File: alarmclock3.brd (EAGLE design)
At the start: 81 x 80 mm, 28 parts, among them X1 MKDSN1,5/2-5,08, X2 MKDSN1,5/2-5,08

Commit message: route 100%
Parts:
- removed C1: (no value), SparkFun-Passives:CPOL-RADIAL-1000UF-63V
- added C11: 330uF/25V, SparkFun-Passives:CPOL-RADIAL-10UF-25V
- moved C10 15.7 mm to (34.5, 30.5)
- moved C4 8.89 mm to (25.4, 22.9)
- moved R5 3.45 mm to (28.7, 26.9)
- moved R2 2.54 mm to (38.1, 30.5)
- moved C14 2.54 mm to (25.4, 49.5)
- moved C9 2.54 mm to (33.0, 50.8)
- moved C8 2.40 mm to (27.9, 49.0)
- moved C13 2.18 mm to (31.8, 26.2)
- moved C7 1.27 mm to (29.7, 30.7)
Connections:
- net GND: now also C11.2; no longer C1.2
- net N$3: now also C11.1; no longer C1.1
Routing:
- net N$2: track 122.7 -> 49.8 mm
- net N$1: track 0.00 -> 58.3 mm, vias 0 -> 1
- net GND: track 297.0 -> 241.2 mm
- net N$27: track 8.62 -> 61.0 mm
- net N$23: track 77.9 -> 29.6 mm, vias 0 -> 2
- net N$8: track 2.54 -> 30.9 mm, vias 0 -> 1
- net N$3: track 114.3 -> 97.5 mm
- net N$25: track 17.4 -> 1.86 mm
- net N$12: track 0.00 -> 13.6 mm, vias 0 -> 2
- net N$6: track 47.5 -> 55.3 mm, vias 1 -> 2
- net VCC: track 53.8 -> 60.4 mm, vias 0 -> 2
- net N$10: track 29.9 -> 36.4 mm, vias 0 -> 2
- net N$11: track 0.00 -> 6.11 mm
- net N$22: track 4.03 -> 9.95 mm
- net N$13: track 28.0 -> 33.5 mm
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
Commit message: !00% routable
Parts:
- moved U$1 6.90 mm to (14.5, 70.6), turned to 270 degrees
- moved U$4 6.86 mm to (65.0, 17.0)
- moved U$2 6.61 mm to (24.4, 72.6)
- moved U$5 6.61 mm to (6.10, 47.2)
- moved C6 3.31 mm to (65.0, 35.1)
- moved X2 2.84 mm to (71.6, 35.8)
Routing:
- net N$27: track 61.0 -> 15.2 mm, vias 2 -> 4
- net N$4: track 88.1 -> 50.0 mm
- net N$10: track 36.4 -> 73.6 mm, vias 2 -> 0
- net N$1: track 58.3 -> 81.5 mm, vias 1 -> 3
- net N$8: track 30.9 -> 37.0 mm
- net N$6: track 55.3 -> 60.6 mm
- net N$18: track 16.2 -> 20.0 mm
- net N$15: track 5.26 -> 8.45 mm, vias 0 -> 2
- net N$17: track 4.73 -> 7.39 mm, vias 0 -> 2
- net GND: track 241.2 -> 243.8 mm
- net N$5: track 49.5 -> 47.0 mm
- net N$23: track 29.6 -> 28.2 mm
- net N$9: track 16.1 -> 15.0 mm
- net N$16: track 37.7 -> 36.6 mm, vias 3 -> 2
- net N$3: track 97.5 -> 98.5 mm
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
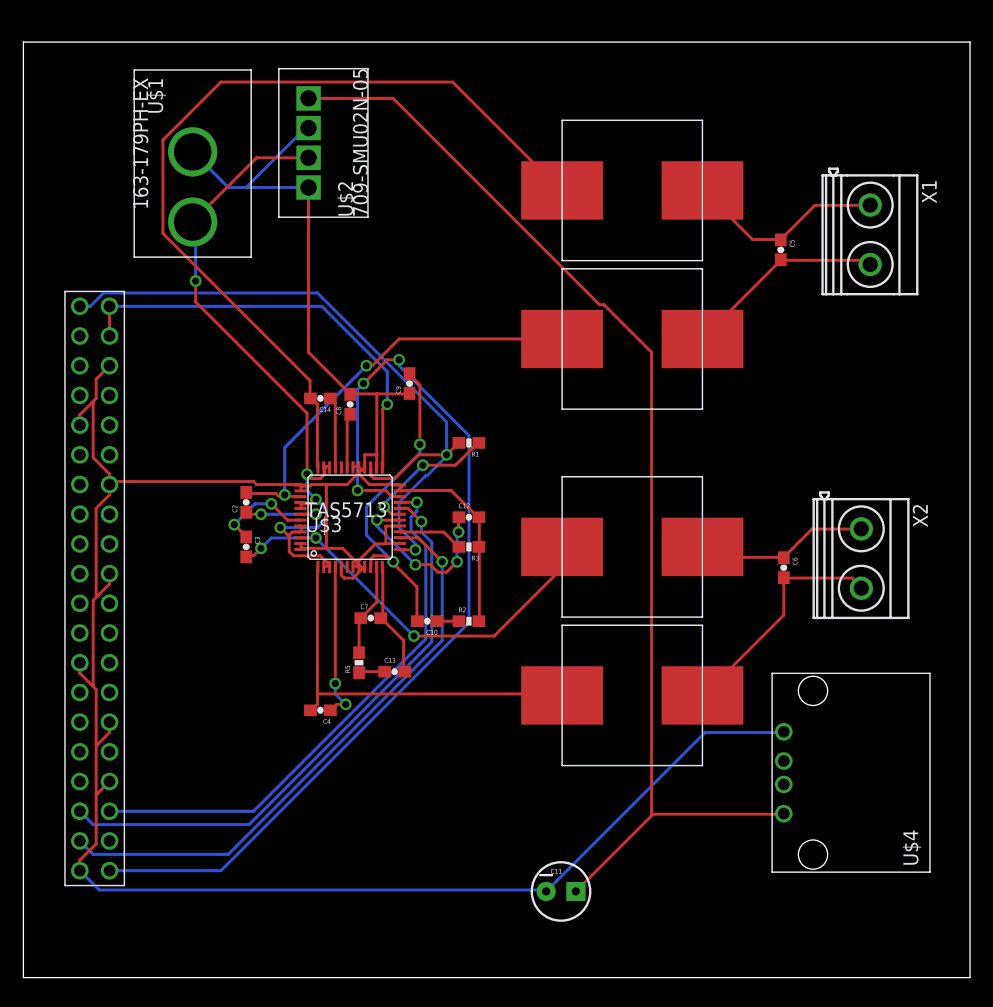
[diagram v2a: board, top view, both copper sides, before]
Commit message: - separate gnd from 18v stage and 3.3v stage - add 2 gpio as terminal block (2 external push button) - complete the bom
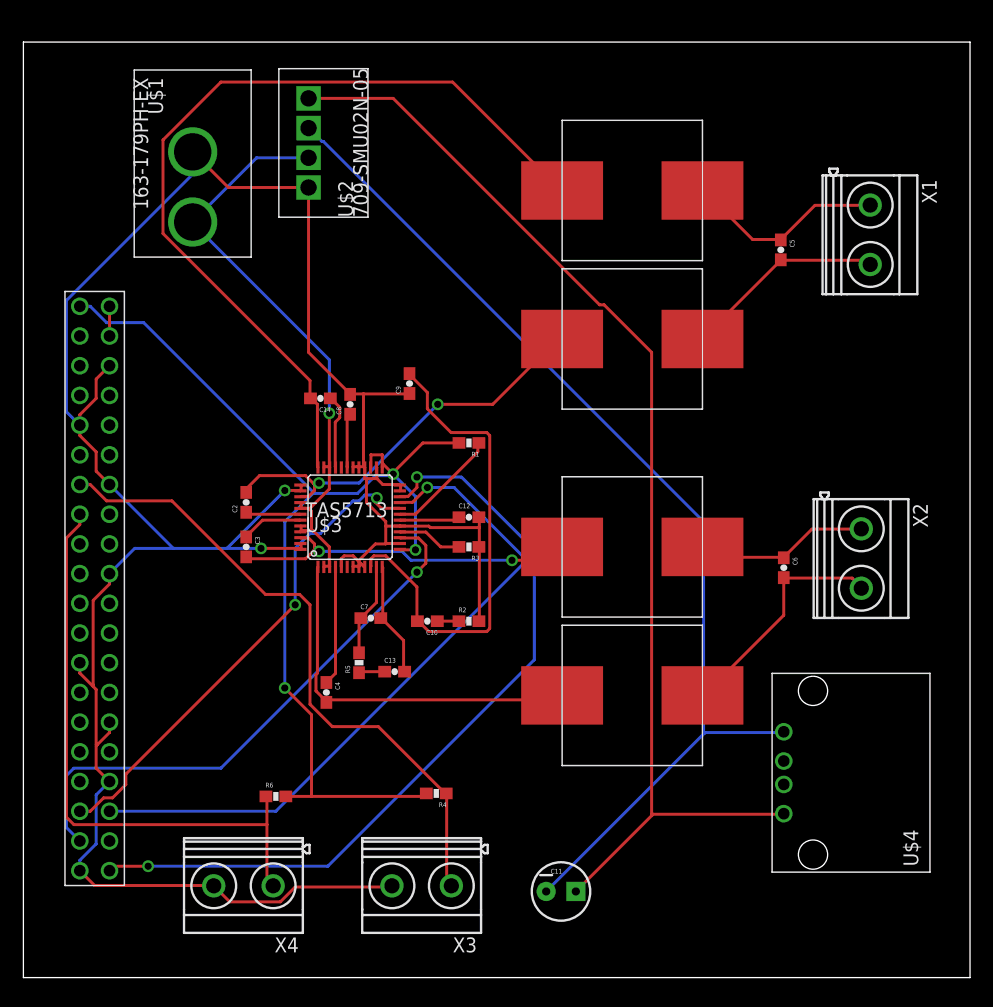
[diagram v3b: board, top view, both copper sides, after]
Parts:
- added R4, R6: 10k, SparkFun-Passives:0603-RES
- added X3, X4: MKDSN1,5/2-5,08, con-phoenix-508:MKDSN1,5/2-5,08
- moved C4 1.61 mm to (25.9, 24.4), turned to 270 degrees
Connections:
- new net +3V3: R1.2, R4.2, R6.2, U$3.P$13, U$3.P$25, U$3.P$27, U$5.P$1
- new net +5V: U$5.P$2, U$5.P$4
- new net N$29: C11.2, U$2.VO-, U$4.P$4
- net GND: now also X3.2, X4.2; no longer C11.2, U$2.VO-, U$4.P$4
- net N$6: now also R6.1, U$5.P$15, X4.1; no longer R1.2, U$3.P$13, U$3.P$27, U$5.P$1
- net N$8: now also R4.1, U$5.P$13, X3.1; no longer U$3.P$25, U$5.P$2, U$5.P$4
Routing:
- net +3V3: track 0.00 -> 94.4 mm, vias 0 -> 3
- net N$29: track 0.00 -> 91.9 mm
- net GND: track 243.8 -> 216.2 mm, vias 0 -> 2
- net N$8: track 37.0 -> 55.4 mm, vias 1 -> 0
- net N$23: track 28.2 -> 41.9 mm, vias 2 -> 0
- net N$1: track 81.5 -> 68.5 mm, vias 3 -> 2
- net N$5: track 47.0 -> 58.2 mm
- net N$27: track 15.2 -> 5.17 mm, vias 4 -> 0
- net N$6: track 60.6 -> 51.7 mm, vias 2 -> 0
- net VCC: track 60.4 -> 52.0 mm, vias 4 -> 1
- net N$4: track 50.0 -> 42.8 mm, vias 1 -> 2
- net N$14: track 36.8 -> 30.3 mm, vias 3 -> 2
- net N$12: track 13.6 -> 10.2 mm, vias 2 -> 0
- net N$15: track 8.45 -> 5.26 mm, vias 2 -> 0
- net N$17: track 7.39 -> 4.73 mm, vias 2 -> 0
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
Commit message: put the 40 pin headers in the correct direction
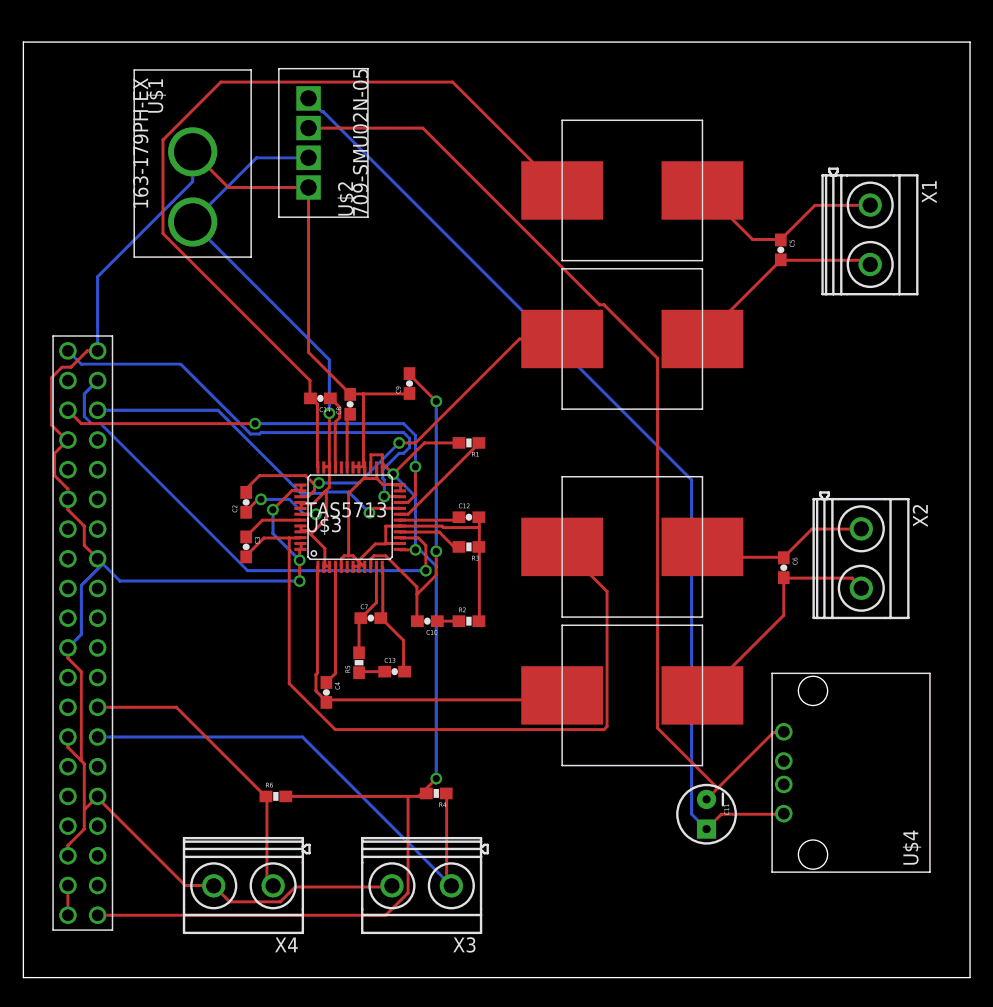
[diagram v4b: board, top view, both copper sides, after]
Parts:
- moved U$5 31.8 mm to (5.08, 15.5), turned to 180 degrees
- moved C11 14.1 mm to (58.4, 14.0), turned to 270 degrees
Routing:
- net N$14: track 30.3 -> 63.7 mm, vias 2 -> 0
- net N$1: track 68.5 -> 39.9 mm, vias 2 -> 1
- net N$6: track 51.7 -> 25.5 mm
- net N$5: track 58.2 -> 37.3 mm, vias 1 -> 2
- net N$3: track 98.5 -> 83.8 mm
- net N$4: track 42.8 -> 29.7 mm, vias 2 -> 1
- net N$23: track 41.9 -> 29.3 mm, vias 0 -> 2
- net N$8: track 55.4 -> 43.6 mm
- net N$29: track 91.9 -> 85.9 mm
- net N$2: track 48.3 -> 42.9 mm
- net +3V3: track 94.4 -> 90.5 mm
- net N$17: track 4.73 -> 8.33 mm, vias 0 -> 2
- net GND: track 216.2 -> 217.9 mm, vias 2 -> 3
- net VCC: track 52.0 -> 53.7 mm

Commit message: add extension to the skywriter (https://www.modmypi.com/raspberry-pi/breakout-boards/pimoroni/pimoroni-skywriter)
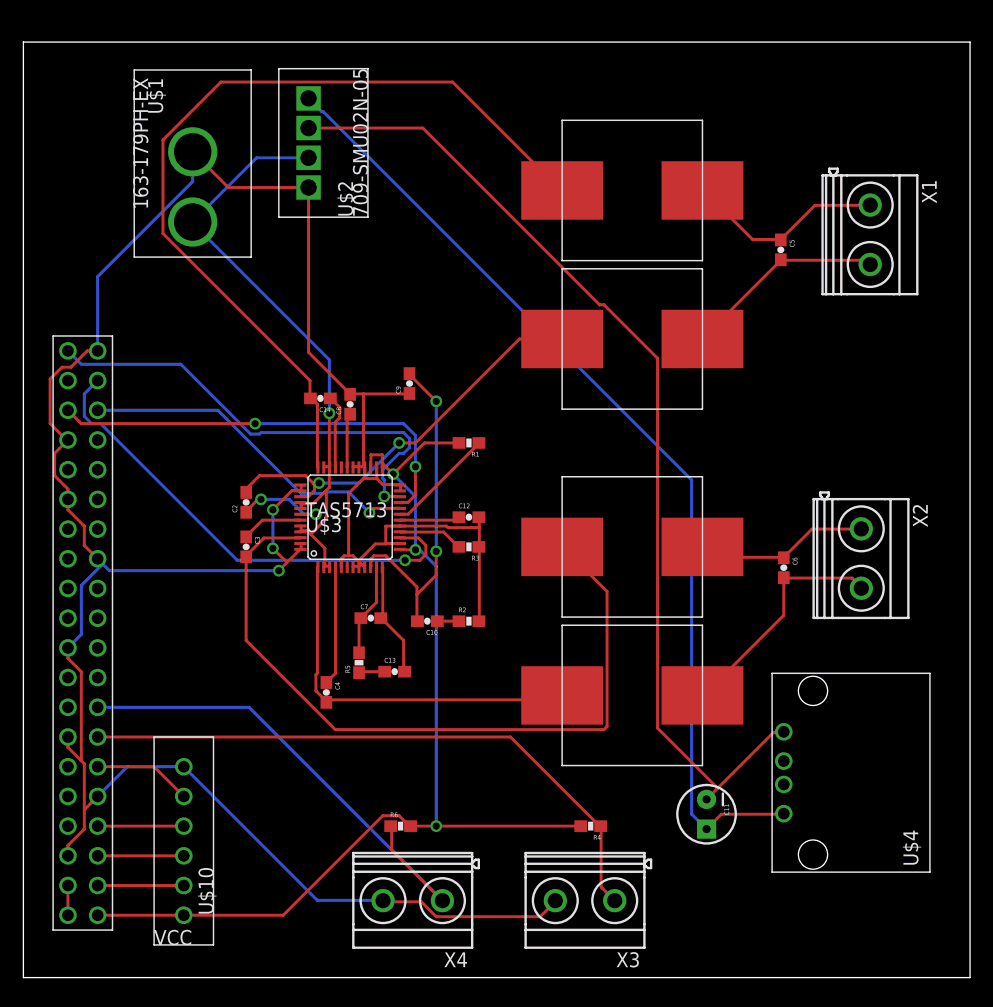
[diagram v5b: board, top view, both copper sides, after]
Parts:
- added U$10: SKYWRITER, skywriter:SKYWRITER_DIM
- moved X4 14.5 mm to (33.3, 6.60)
- moved X3 14.0 mm to (48.0, 6.60)
- moved R4 13.5 mm to (48.5, 13.0)
- moved R6 11.0 mm to (32.3, 13.0)
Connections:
- new net N$30: U$10.SDA, U$5.P$3
- new net N$31: U$10.SCL, U$5.P$5
- new net N$32: U$10.RESET, U$5.P$7
- new net N$33: U$10.TRFR, U$5.P$11
- net +3V3: now also U$10.VCC
- net GND: now also U$10.GND
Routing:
- net N$6: track 25.5 -> 44.6 mm
- net GND: track 217.9 -> 232.0 mm
- net N$8: track 43.6 -> 53.1 mm
- net N$33: track 0.00 -> 8.42 mm
- net N$32: track 0.00 -> 7.37 mm
- net N$31: track 0.00 -> 7.37 mm
- net N$30: track 0.00 -> 7.37 mm
- net N$2: track 42.9 -> 41.3 mm
- net +3V3: track 90.5 -> 89.9 mm
